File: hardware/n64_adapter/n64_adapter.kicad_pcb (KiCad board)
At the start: 2 copper layers, 96.6 x 25.5 mm, 7 parts, among them J1 N64_Slot, J2 CART SLOT TOP ROW, J3 CART SLOT BOTTOM ROW, J4 Conn_01x01, J5 Conn_01x01, J6 Conn_01x01

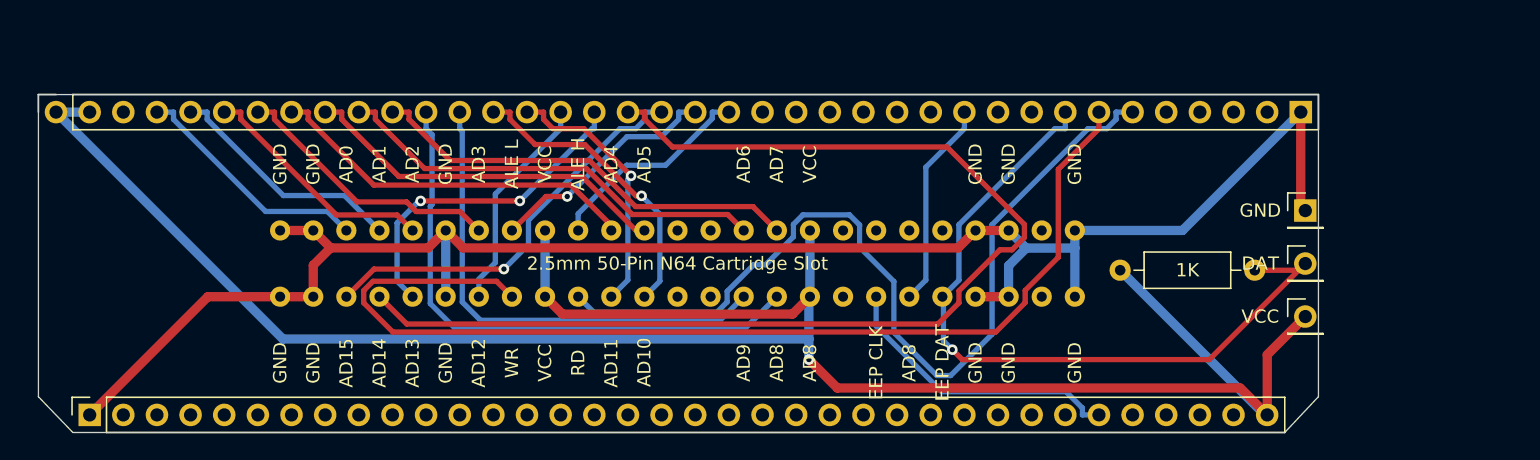
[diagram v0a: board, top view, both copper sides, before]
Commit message: Update N64 breakout
add controller port to schematic and board. change board to inch standard, minimize trace width and reroute all traces. realign bottom silkscreen to pins.
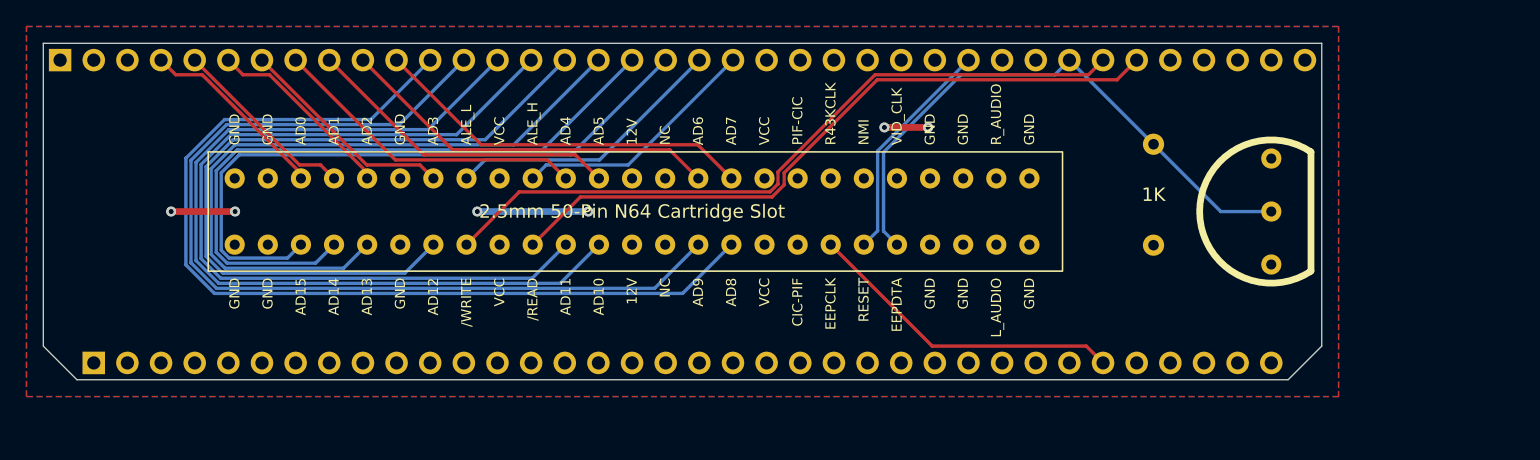
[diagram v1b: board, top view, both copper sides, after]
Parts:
- removed J5, J6: Conn_01x01, Connector_PinHeader_2.54mm:PinHeader_1x01_P2.54mm_Vertical
- J1: value N64_Slot -> CART SLOT TOP ROW; footprint !sanni:N64 Slot -> Connector_PinHeader_2.54mm:PinHeader_1x38_P2.54mm_Vertical; moved to B.Cu
- J2: value CART SLOT TOP ROW -> CART SLOT BOTTOM ROW; footprint Connector_PinSocket_2.54mm:PinSocket_1x38_P2.54mm_Vertical -> Connector_PinHeader_2.54mm:PinHeader_1x36_P2.54mm_Vertical; moved to B.Cu
- J3: value CART SLOT BOTTOM ROW -> N64_Slot; footprint Connector_PinSocket_2.54mm:PinSocket_1x36_P2.54mm_Vertical -> !OSCR:N64 Slot
- J4: value Conn_01x01 -> N64_Controller_Port; footprint Connector_PinHeader_2.54mm:PinHeader_1x01_P2.54mm_Vertical -> !OSCR:N64_CONTROLLER_PORT
- R1: footprint Resistor_THT:R_Axial_DIN0207_L6.3mm_D2.5mm_P10.16mm_Horizontal -> Resistor_THT:R_Axial_DIN0207_L6.3mm_D2.5mm_P7.62mm_Horizontal; moved to B.Cu
- moved J3 43.7 mm to (146.1, 88.9)
- moved J1 24.4 mm to (102.9, 77.5), turned to -90 degrees
- moved J2 19.1 mm to (105.4, 100.3), turned to -90 degrees
- moved R1 3.15 mm to (185.4, 91.4), turned to 90 degrees
- moved J4 2.57 mm to (194.3, 88.9), turned to 90 degrees
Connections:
- J1 pad 1: GND -> VCC
- J1 pad 10: D9 -> A6
- J1 pad 11: A11 -> A7
- J1 pad 12: A10 -> A8
- J1 pad 13: unconnected-(J1-Pad13) -> A9
- J1 pad 14: unconnected-(J1-Pad14) -> A10
- J1 pad 15: A9 -> A11
- J1 pad 16: A8 -> A12
- J1 pad 17: VCC -> A13
- J1 pad 18: unconnected-(J1-Pad18) -> A14
- J1 pad 19: CLK1 -> A15
- J1 pad 2: GND -> VCC
- J1 pad 20: D17 -> D37
- J1 pad 21: D7 -> D36
- J1 pad 22: GND -> D35
- J1 pad 23: GND -> D34
- J1 pad 24: unconnected-(J1-Pad24) -> D33
- J1 pad 25: GND -> D32
- J1 pad 26: GND -> D31
- J1 pad 27: GND -> D30
- J1 pad 28: A0 -> D17
- J1 pad 29: A1 -> D16
- J1 pad 3: A15 -> unconnected-(J1-Pad3)
- J1 pad 30: A2 -> D6
- J1 pad 31: GND -> D7
- J1 pad 32: A3 -> D8
- J1 pad 33: D37 -> D9
- J1 pad 34: VCC -> SS
- J1 pad 35: D36 -> SCK
- J1 pad 36: A4 -> MOSI
- J1 pad 37: A5 -> MISO
- J1 pad 38: unconnected-(J1-Pad38) -> GND
- J1 pad 4: A14 -> A0
- J1 pad 5: A13 -> A1
- J1 pad 6: GND -> A2
- J1 pad 7: A12 -> A3
- J1 pad 8: D8 -> A4
- J1 pad 9: VCC -> A5
- J2 pad 1: VCC -> GND
- J2 pad 10: A6 -> D15
- J2 pad 11: A7 -> D14
- J2 pad 12: A8 -> D22
- J2 pad 13: A9 -> D23
- J2 pad 14: A10 -> D24
- J2 pad 15: A11 -> D25
- J2 pad 16: A12 -> D26
- J2 pad 17: A13 -> D27
- J2 pad 18: A14 -> D28
- J2 pad 19: A15 -> D29
- J2 pad 2: VCC -> D0
- J2 pad 20: D37 -> D49
- J2 pad 21: D36 -> D48
- J2 pad 22: D35 -> D47
- J2 pad 23: D34 -> D46
- J2 pad 24: D33 -> D45
- J2 pad 25: D32 -> D44
- J2 pad 26: D31 -> D43
- J2 pad 27: D30 -> D42
- J2 pad 28: D17 -> SDA
- J2 pad 29: D16 -> SCL
- J2 pad 3: +5V -> D1
- J2 pad 30: D6 -> CLK2
- J2 pad 31: D7 -> CLK1
- J2 pad 32: D8 -> CLK0
- J2 pad 33: D9 -> D13
- J2 pad 34: D53 -> D38
- J2 pad 35: D52 -> RESET
- J2 pad 36: D51 -> VCC
- J2 pad 4: A0 -> D5
- J2 pad 5: A1 -> D2
- J2 pad 6: A2 -> D3
- J2 pad 7: A3 -> D41
- J2 pad 8: A4 -> D40
- J2 pad 9: A5 -> D4
- J3 pad 10: D15 -> D9
- J3 pad 11: D14 -> A11
- J3 pad 12: D22 -> A10
- J3 pad 13: D23 -> unconnected-(J3-Pad13)
- J3 pad 14: D24 -> unconnected-(J3-Pad14)
- J3 pad 15: D25 -> A9
- J3 pad 16: D26 -> A8
- J3 pad 17: D27 -> VCC
- J3 pad 18: D28 -> unconnected-(J3-Pad18)
- J3 pad 19: D29 -> CLK1
- J3 pad 2: D0 -> GND
- J3 pad 20: D49 -> D17
- J3 pad 21: D48 -> D7
- J3 pad 22: D47 -> GND
- J3 pad 23: D46 -> GND
- J3 pad 24: D45 -> unconnected-(J3-Pad24)
- J3 pad 25: D44 -> GND
- J3 pad 26: D43 -> GND
- J3 pad 27: D42 -> GND
- J3 pad 28: D20 -> A0
- J3 pad 29: D21 -> A1
- J3 pad 3: D1 -> A15
- J3 pad 30: CLK2 -> A2
- J3 pad 31: CLK1 -> GND
- J3 pad 32: CLK0 -> A3
- J3 pad 33: D13 -> D37
- J3 pad 34: D38 -> VCC
- J3 pad 35: RESET -> D36
- J3 pad 36: VCC -> A4
- J3 pad 4: D5 -> A14
- J3 pad 5: D2 -> A13
- J3 pad 6: D3 -> GND
- J3 pad 7: D41 -> A12
- J3 pad 8: D40 -> D8
- J3 pad 9: D4 -> VCC
- J4 pad 1: GND -> VCC
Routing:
- net VCC: track 162.9 -> 8.13 mm, vias 1 -> 4
- net GND: track 132.6 -> 8.38 mm, vias 0 -> 2
- net A11: track 19.9 -> 64.5 mm, vias 1 -> 0
- net A10: track 22.8 -> 65.7 mm, vias 1 -> 0
- net A12: track 16.5 -> 55.8 mm
- net A14: track 87.5 -> 50.8 mm
- net A9: track 37.0 -> 71.9 mm
- net A8: track 42.6 -> 73.2 mm
- net D8: track 81.4 -> 54.4 mm
- net A13: track 25.1 -> 52.1 mm, vias 2 -> 0
- net A15: track 31.0 -> 49.6 mm, vias 1 -> 0
- net D9: track 68.1 -> 51.9 mm
- net D7: track 56.5 -> 44.3 mm, vias 1 -> 0
- net A4: track 28.4 -> 24.1 mm
- net A1: track 18.3 -> 14.2 mm
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- added copper zone on F.Cu, net GND
- added copper zone on B.Cu, net VCC
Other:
- board size 96.6 x 25.5 mm -> 96.5 x 25.4 mm
- board text removed: "2.5mm 50-Pin N64 Cartridge Slot"
- board text removed: "AD0"
- board text removed: "AD1"
- board text removed: "AD10"
- board text removed: "AD11"
- board text removed: "AD12"
- board text removed: "AD13"
- board text removed: "AD14"
- board text removed: "AD15"
- board text removed: "AD2"
- board text removed: "AD3"
- board text removed: "AD4"
- board text removed: "AD5"
- board text removed: "AD6"
- board text removed: "AD7"
- board text removed: "AD8"
- board text removed: "AD9"
- board text removed: "ALE H"
- board text removed: "ALE L"
- board text removed: "EEP CLK"
- board text removed: "EEP DAT"
- board text removed: "RD"
- board text removed: "WR"

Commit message: finalize n64 breakout design
Ready for RTM
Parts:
- R1: footprint Resistor_THT:R_Axial_DIN0207_L6.3mm_D2.5mm_P7.62mm_Horizontal -> Resistor_THT:R_Axial_DIN0207_L6.3mm_D2.5mm_P10.16mm_Horizontal
- moved R1 15.5 mm to (200.7, 94.0)
- moved J4 12.7 mm to (207.0, 88.9)
- moved J3 9.65 mm to (136.4, 88.9)
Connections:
- J1 pad 22: D35 -> unconnected-(J1-Pin_22-Pad22)
- J1 pad 23: D34 -> unconnected-(J1-Pin_23-Pad23)
- J1 pad 24: D33 -> unconnected-(J1-Pin_24-Pad24)
- J1 pad 25: D32 -> unconnected-(J1-Pin_25-Pad25)
- J1 pad 26: D31 -> unconnected-(J1-Pin_26-Pad26)
- J1 pad 27: D30 -> unconnected-(J1-Pin_27-Pad27)
- J1 pad 29: D16 -> unconnected-(J1-Pin_29-Pad29)
- J1 pad 30: D6 -> unconnected-(J1-Pin_30-Pad30)
- J1 pad 34: SS -> unconnected-(J1-Pin_34-Pad34)
- J1 pad 35: SCK -> unconnected-(J1-Pin_35-Pad35)
- J1 pad 36: MOSI -> unconnected-(J1-Pin_36-Pad36)
- J1 pad 37: MISO -> unconnected-(J1-Pin_37-Pad37)
- J2 pad 10: D15 -> unconnected-(J2-Pin_10-Pad10)
- J2 pad 11: D14 -> unconnected-(J2-Pin_11-Pad11)
- J2 pad 12: D22 -> unconnected-(J2-Pin_12-Pad12)
- J2 pad 13: D23 -> unconnected-(J2-Pin_13-Pad13)
- J2 pad 14: D24 -> unconnected-(J2-Pin_14-Pad14)
- J2 pad 15: D25 -> unconnected-(J2-Pin_15-Pad15)
- J2 pad 16: D26 -> unconnected-(J2-Pin_16-Pad16)
- J2 pad 17: D27 -> unconnected-(J2-Pin_17-Pad17)
- J2 pad 18: D28 -> unconnected-(J2-Pin_18-Pad18)
- J2 pad 19: D29 -> unconnected-(J2-Pin_19-Pad19)
- J2 pad 2: D0 -> unconnected-(J2-Pin_2-Pad2)
- J2 pad 20: D49 -> unconnected-(J2-Pin_20-Pad20)
- J2 pad 21: D48 -> unconnected-(J2-Pin_21-Pad21)
- J2 pad 22: D47 -> unconnected-(J2-Pin_22-Pad22)
- J2 pad 23: D46 -> unconnected-(J2-Pin_23-Pad23)
- J2 pad 24: D45 -> unconnected-(J2-Pin_24-Pad24)
- J2 pad 25: D44 -> unconnected-(J2-Pin_25-Pad25)
- J2 pad 26: D43 -> unconnected-(J2-Pin_26-Pad26)
- J2 pad 27: D42 -> unconnected-(J2-Pin_27-Pad27)
- J2 pad 28: SDA -> unconnected-(J2-Pin_28-Pad28)
- J2 pad 29: SCL -> unconnected-(J2-Pin_29-Pad29)
- J2 pad 3: D1 -> unconnected-(J2-Pin_3-Pad3)
- J2 pad 30: CLK2 -> unconnected-(J2-Pin_30-Pad30)
- J2 pad 32: CLK0 -> unconnected-(J2-Pin_32-Pad32)
- J2 pad 33: D13 -> unconnected-(J2-Pin_33-Pad33)
- J2 pad 34: D38 -> unconnected-(J2-Pin_34-Pad34)
- J2 pad 35: RESET -> unconnected-(J2-Pin_35-Pad35)
- J2 pad 4: D5 -> unconnected-(J2-Pin_4-Pad4)
- J2 pad 5: D2 -> unconnected-(J2-Pin_5-Pad5)
- J2 pad 6: D3 -> unconnected-(J2-Pin_6-Pad6)
- J2 pad 7: D41 -> unconnected-(J2-Pin_7-Pad7)
- J2 pad 8: D40 -> unconnected-(J2-Pin_8-Pad8)
- J2 pad 9: D4 -> unconnected-(J2-Pin_9-Pad9)
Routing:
- net D7: track 44.3 -> 62.7 mm
- net D8: track 54.4 -> 66.0 mm
- net D9: track 51.9 -> 63.6 mm
- net A12: track 55.8 -> 65.8 mm
- net A9: track 71.9 -> 82.0 mm
- net A8: track 73.2 -> 83.2 mm
- net A13: track 52.1 -> 62.1 mm
- net A15: track 49.6 -> 59.7 mm
- net A14: track 50.8 -> 60.9 mm
- net A10: track 65.7 -> 75.8 mm
- net A11: track 64.5 -> 74.5 mm
- net A7: track 29.0 -> 19.2 mm
- net A5: track 24.1 -> 14.3 mm
- net A6: track 29.0 -> 19.3 mm
- net A4: track 24.1 -> 14.3 mm
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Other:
- board size 96.5 x 25.4 mm -> 107.7 x 25.4 mm
- board text removed: "DAT"
